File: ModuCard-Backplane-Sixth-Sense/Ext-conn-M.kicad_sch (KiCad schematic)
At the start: 1 part, among them J1 09031967921

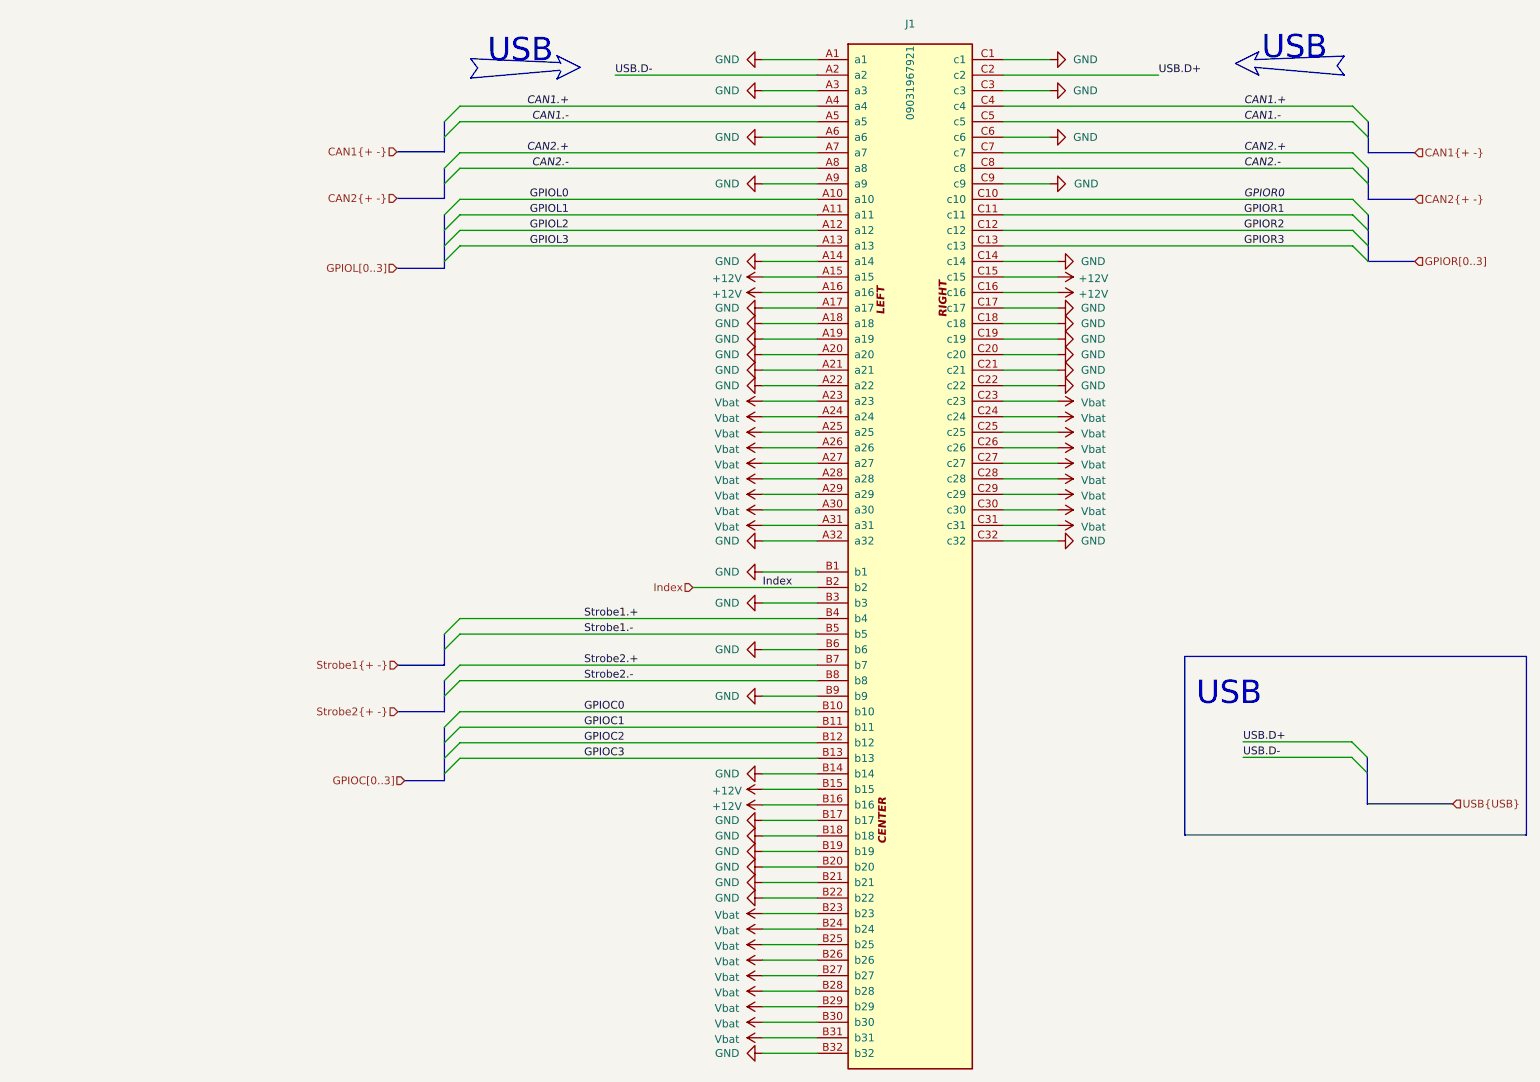
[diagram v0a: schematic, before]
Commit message: fix DRC errors, change pinout
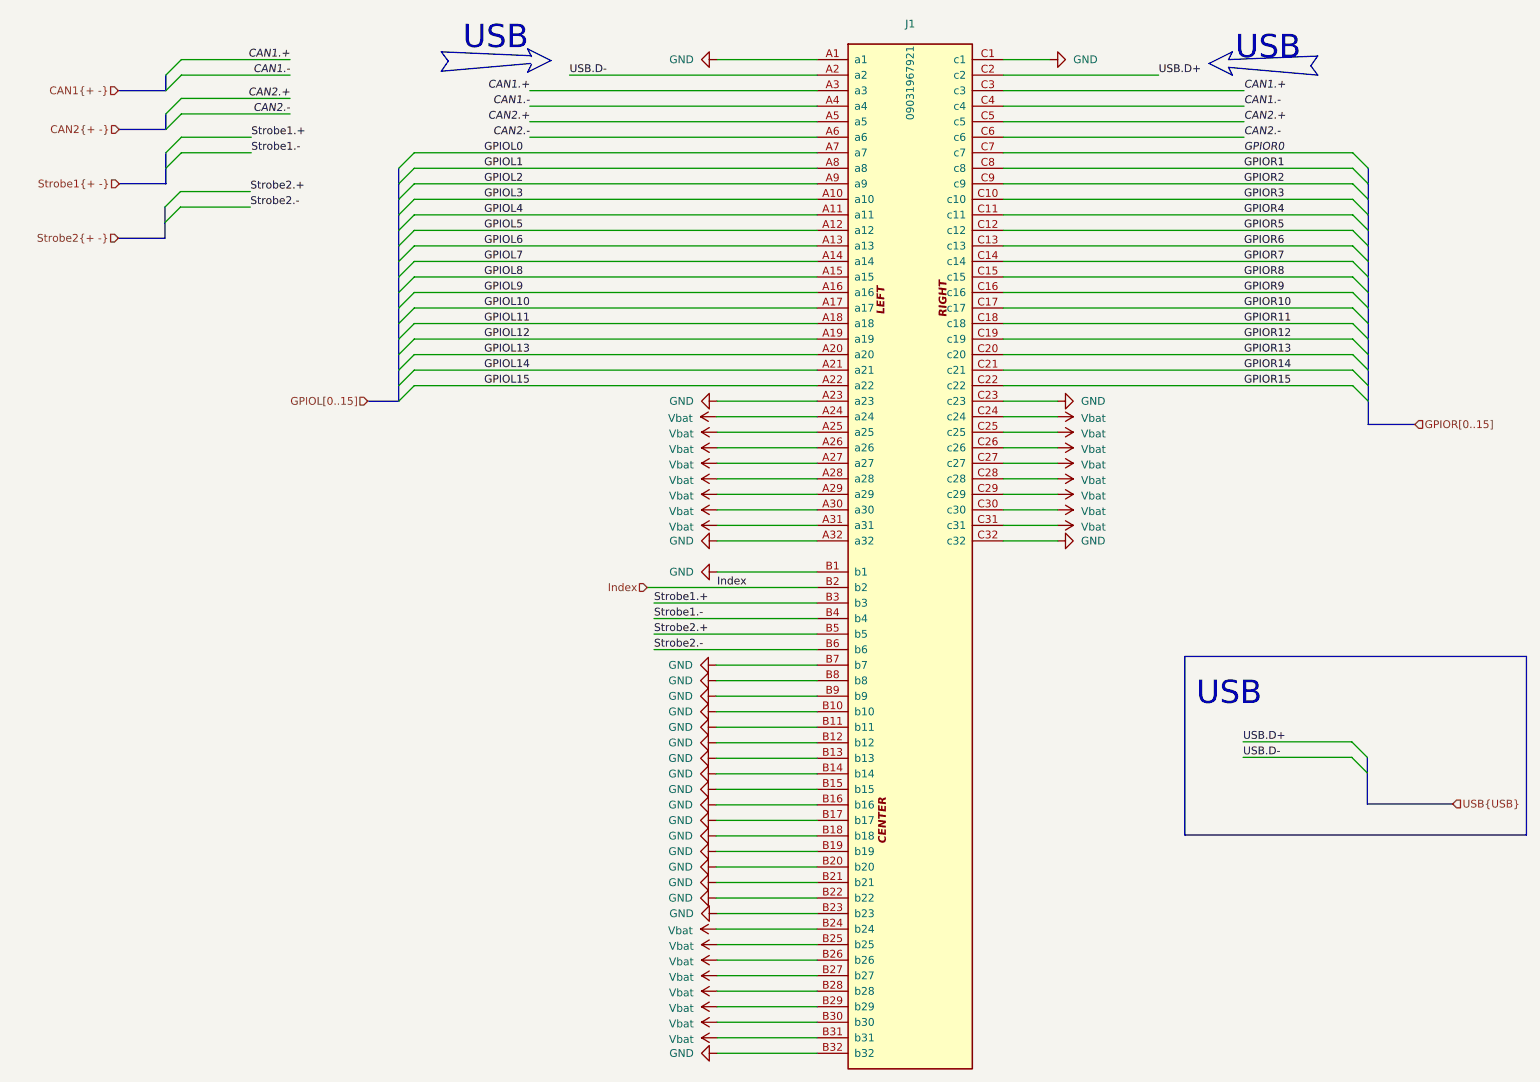
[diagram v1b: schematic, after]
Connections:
- net GPIOC0 is gone; now on net GND: J1.B10 (b10)
- net GPIOC1 is gone; now on net GND: J1.B11 (b11)
- net GPIOC2 is gone; now on net GND: J1.B12 (b12)
- net GPIOC3 is gone; now on net GND: J1.B13 (b13)
- net CAN1.+: now also J1.A3 (a3), J1.C3 (c3); no longer J1.A4 (a4), J1.C4 (c4)
- net CAN1.-: now also J1.A4 (a4), J1.C4 (c4); no longer J1.A5 (a5), J1.C5 (c5)
- net CAN2.+: now also J1.A5 (a5), J1.C5 (c5); no longer J1.A7 (a7), J1.C7 (c7)
- net CAN2.-: now also J1.A6 (a6), J1.C6 (c6); no longer J1.A8 (a8), J1.C8 (c8)
- net GND: now also J1.A23 (a23), J1.B15 (b15), J1.B16 (b16), J1.B23 (b23), J1.B7 (b7), J1.B8 (b8), J1.C23 (c23); no longer J1.A14 (a14), J1.A17 (a17), J1.A18 (a18), J1.A19 (a19), J1.A20 (a20), J1.A21 (a21), J1.A22 (a22), J1.A3 (a3), J1.A6 (a6), J1.A9 (a9), J1.B3 (b3), J1.B6 (b6), J1.C14 (c14), J1.C17 (c17), J1.C18 (c18), J1.C19 (c19), J1.C20 (c20), J1.C21 (c21), J1.C22 (c22), J1.C3 (c3), J1.C6 (c6), J1.C9 (c9)
- net GPIOL0: now also J1.A7 (a7); no longer J1.A10 (a10)
- net GPIOL1: now also J1.A8 (a8); no longer J1.A11 (a11)
- net GPIOL2: now also J1.A9 (a9); no longer J1.A12 (a12)
- net GPIOL3: now also J1.A10 (a10); no longer J1.A13 (a13)
- net GPIOR0: now also J1.C7 (c7); no longer J1.C10 (c10)
- net GPIOR1: now also J1.C8 (c8); no longer J1.C11 (c11)
- net GPIOR2: now also J1.C9 (c9); no longer J1.C12 (c12)
- net GPIOR3: now also J1.C10 (c10); no longer J1.C13 (c13)
- net Strobe1.+: now also J1.B3 (b3); no longer J1.B4 (b4)
- net Strobe1.-: now also J1.B4 (b4); no longer J1.B5 (b5)
- net Strobe2.+: now also J1.B5 (b5); no longer J1.B7 (b7)
- net Strobe2.-: now also J1.B6 (b6); no longer J1.B8 (b8)
- net Vbat: no longer J1.A23 (a23), J1.B23 (b23), J1.C23 (c23)
- removed net +12V: J1.A15 (a15), J1.A16 (a16), J1.B15 (b15), J1.B16 (b16), J1.C15 (c15), J1.C16 (c16)
- new net GPIOL10: J1.A17 (a17)
- new net GPIOL11: J1.A18 (a18)
- new net GPIOL12: J1.A19 (a19)
- new net GPIOL13: J1.A20 (a20)
- new net GPIOL14: J1.A21 (a21)
- new net GPIOL15: J1.A22 (a22)
- new net GPIOL4: J1.A11 (a11)
- new net GPIOL5: J1.A12 (a12)
- new net GPIOL6: J1.A13 (a13)
- new net GPIOL7: J1.A14 (a14)
- new net GPIOL8: J1.A15 (a15)
- new net GPIOL9: J1.A16 (a16)
- new net GPIOR10: J1.C17 (c17)
- new net GPIOR11: J1.C18 (c18)
- new net GPIOR12: J1.C19 (c19)
- new net GPIOR13: J1.C20 (c20)
- new net GPIOR14: J1.C21 (c21)
- new net GPIOR15: J1.C22 (c22)
- new net GPIOR4: J1.C11 (c11)
- new net GPIOR5: J1.C12 (c12)
- new net GPIOR6: J1.C13 (c13)
- new net GPIOR7: J1.C14 (c14)
- new net GPIOR8: J1.C15 (c15)
- new net GPIOR9: J1.C16 (c16)

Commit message: project overhaul
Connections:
- net GND: no longer J1.B1 (b1)
- net Index renamed Index2
- new net Index1: J1.B1 (b1)
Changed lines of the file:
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@@
 	)
 	(bus_entry
-		(at 23.0124 25.4)
+		(at 53.4924 137.16)
 		(size -2.54 2.54)
 		(stroke
@@
 	)
 	(bus_entry
-		(at 23.0124 22.86)
+		(at 53.4924 134.62)
 		(size -2.54 2.54)
 		(stroke
@@
 	)
 	(bus_entry
-		(at 20.4724 40.64)
+		(at 50.9524 152.4)
 		(size 2.54 -2.54)
 		(stroke
@@
 	)
 	(bus_entry
-		(at 20.32 49.53)
+		(at 50.8 161.29)
 		(size 2.54 -2.54)
 		(stroke
@@
 	)
 	(bus_entry
-		(at 20.32 46.99)
+		(at 50.8 158.75)
 		(size 2.54 -2.54)
 		(stroke
@@
 	)
 	(bus_entry
-		(at 23.0124 29.21)
+		(at 53.4924 140.97)
 		(size -2.54 2.54)
 		(stroke
@@
 	)
 	(bus_entry
-		(at 20.4724 38.1)
+		(at 50.9524 149.86)
 		(size 2.54 -2.54)
 		(stroke
@@
 	)
 	(bus_entry
-		(at 23.0124 31.75)
+		(at 53.4924 143.51)
 		(size -2.54 2.54)
 		(stroke
@@
 	(bus
 		(pts
-			(xy 12.8524 27.94) (xy 20.4724 27.94)
+			(xy 43.3324 139.7) (xy 50.9524 139.7)
 		)
 		(stroke
@@
 	(wire
 		(pts
+			(xy 99.2124 109.22) (xy 127 109.22)
+		)
+		(stroke
+			(width 0)
+			(type default)
+		)
+	)
+	(wire
+		(pts
 			(xy 166.37 99.06) (xy 157.48 99.06)
 		)
@@
 	(bus
 		(pts
-			(xy 20.4724 31.75) (xy 20.4724 34.29)
+			(xy 50.9524 143.51) (xy 50.9524 146.05)
 		)
 		(stroke
@@
 	(bus
 		(pts
-			(xy 20.32 46.99) (xy 20.32 49.53)
+			(xy 50.8 158.75) (xy 50.8 161.29)
 		)
 		(stroke
@@
 	(wire
 		(pts
-			(xy 23.0124 25.4) (xy 40.7924 25.4)
+			(xy 53.4924 137.16) (xy 71.2724 137.16)
 		)
 		(stroke
@@
 	(wire
 		(pts
-			(xy 23.0124 38.1) (xy 34.4424 38.1)
+			(xy 53.4924 149.86) (xy 64.9224 149.86)
 		)
 		(stroke
@@
 	(bus
 		(pts
-			(xy 20.32 49.53) (xy 20.32 52.07)
+			(xy 50.8 161.29) (xy 50.8 163.83)
 		)
 		(stroke
@@
 	(wire
 		(pts
-			(xy 22.86 44.45) (xy 34.29 44.45)
+			(xy 53.34 156.21) (xy 64.77 156.21)
 		)
 		(stroke
@@
 	(wire
 		(pts
-			(xy 196.85 35.56) (xy 157.48 35.56)
+			(xy 99.06 106.68) (xy 127 106.68)
 		)
 		(stroke
@@
 	(wire
 		(pts
-			(xy 110.49 81.28) (xy 127 81.28)
+			(xy 196.85 35.56) (xy 157.48 35.56)
 		)
 		(stroke
@@
 	(wire
 		(pts
-			(xy 166.37 96.52) (xy 157.48 96.52)
+			(xy 110.49 81.28) (xy 127 81.28)
 		)
 		(stroke
@@
 	(wire
 		(pts
-			(xy 166.37 93.98) (xy 157.48 93.98)
+			(xy 166.37 96.52) (xy 157.48 96.52)
 		)
 		(stroke
@@
 		)
 	)
-	(bus
+	(wire
 		(pts
-			(xy 58.5724 78.74) (xy 53.4924 78.74)
+			(xy 166.37 93.98) (xy 157.48 93.98)
 		)
 		(stroke
@@
 	(bus
 		(pts
-			(xy 12.8524 43.18) (xy 20.4724 43.18)
+			(xy 58.5724 78.74) (xy 53.4924 78.74)
 		)
 		(stroke
@@
 		)
 	)
-	(wire
+	(bus
 		(pts
-			(xy 80.01 27.94) (xy 127 27.94)
+			(xy 43.3324 154.94) (xy 50.9524 154.94)
 		)
 		(stroke
@@
 	(wire
 		(pts
-			(xy 99.2124 109.22) (xy 127 109.22)
+			(xy 80.01 27.94) (xy 127 27.94)
 		)
 		(stroke
@@
 	(wire
 		(pts
-			(xy 23.0124 35.56) (xy 34.4424 35.56)
+			(xy 53.4924 147.32) (xy 64.9224 147.32)
 		)
 		(stroke
@@
 	(bus
 		(pts
-			(xy 20.4724 40.64) (xy 20.4724 43.18)
+			(xy 50.9524 152.4) (xy 50.9524 154.94)
 		)
 		(stroke
@@
 	(wire
 		(pts
-			(xy 22.86 46.99) (xy 34.29 46.99)
+			(xy 53.34 158.75) (xy 64.77 158.75)
 		)
 		(stroke
@@
 	(bus
 		(pts
-			(xy 12.8524 34.29) (xy 20.4724 34.29)
+			(xy 43.3324 146.05) (xy 50.9524 146.05)
 		)
 		(stroke
@@
 	(bus
 		(pts
-			(xy 12.7 52.07) (xy 20.32 52.07)
+			(xy 43.18 163.83) (xy 50.8 163.83)
 		)
 		(stroke
@@
 	(wire
 		(pts
-			(xy 40.7924 29.21) (xy 23.0124 29.21)
+			(xy 71.2724 140.97) (xy 53.4924 140.97)
 		)
 		(stroke
@@
 	(wire
 		(pts
-			(xy 40.7924 31.75) (xy 23.0124 31.75)
-		)
-		(stroke
-			(width 0)
-			(type default)
-		)
-	)
-	(wire
-		(pts
-			(xy 110.6424 106.68) (xy 127 106.68)
+			(xy 71.2724 143.51) (xy 53.4924 143.51)
 		)
 		(stroke
@@
 	(bus
 		(pts
-			(xy 20.4724 38.1) (xy 20.4724 40.64)
+			(xy 50.9524 149.86) (xy 50.9524 152.4)
 		)
 		(stroke
@@
 	(wire
 		(pts
-			(xy 23.0124 22.86) (xy 40.7924 22.86)
+			(xy 53.4924 134.62) (xy 71.2724 134.62)
 		)
 		(stroke
@@
 	(bus
 		(pts
-			(xy 20.4724 25.4) (xy 20.4724 27.94)
+			(xy 50.9524 137.16) (xy 50.9524 139.7)
 		)
 		(stroke
@@
 	)
 	(label "CAN1.+"
-		(at 40.7924 22.86 180)
+		(at 71.2724 134.62 180)
 		(effects
 			(font
@@
 	)
 	(label "Strobe2.-"
-		(at 34.29 46.99 0)
+		(at 64.77 158.75 0)
 		(effects
 			(font
@@
 	)
 	(label "CAN2.-"
-		(at 40.7924 31.75 180)
+		(at 71.2724 143.51 180)
 		(effects
 			(font
@@
 	)
 	(label "CAN1.-"
-		(at 40.7924 25.4 180)
+		(at 71.2724 137.16 180)
 		(effects
 			(font
@@
 	)
 	(label "Strobe1.+"
-		(at 34.4424 35.56 0)
+		(at 64.9224 147.32 0)
 		(effects
 			(font
@@
 	)
 	(label "Strobe1.-"
-		(at 34.4424 38.1 0)
+		(at 64.9224 149.86 0)
 		(effects
 			(font
@@
 	)
 	(label "CAN2.+"
-		(at 40.7924 29.21 180)
+		(at 71.2724 140.97 180)
 		(effects
 			(font
@@
 		)
 	)
+	(label "Index1"
+		(at 100.1776 106.68 0)
+		(effects
+			(font
+				(size 1.27 1.27)
+			)
+			(justify left bottom)
+		)
+	)
 	(label "GPIOR14"
 		(at 196.85 73.66 0)
@@
 		)
 	)
-	(label "Index"
-		(at 110.6424 109.22 0)
+	(label "Index2"
+		(at 100.33 109.22 0)
 		(effects
 			(font
@@
 	)
 	(label "Strobe2.+"
-		(at 34.29 44.45 0)
+		(at 64.77 156.21 0)
 		(effects
 			(font
@@
 	(hierarchical_label "Strobe2{+ -}"
 		(shape input)
-		(at 12.7 52.07 180)
+		(at 43.18 163.83 180)
 		(effects
 			(font
@@
 		)
 	)
-	(hierarchical_label "Index"
-		(shape input)
-		(at 99.2124 109.22 180)
-		(effects
-			(font
-				(size 1.27 1.27)
-			)
-			(justify right)
-		)
-	)
 	(hierarchical_label "CAN2{+ -}"
 		(shape input)
-		(at 12.8524 34.29 180)
+		(at 43.3324 146.05 180)
 		(effects
 			(font
@@
 	(hierarchical_label "Strobe1{+ -}"
 		(shape input)
-		(at 12.8524 43.18 180)
+		(at 43.3324 154.94 180)
+		(effects
+			(font
+				(size 1.27 1.27)
+			)
+			(justify right)
+		)
+	)
+	(hierarchical_label "Index2"
+		(shape bidirectional)
+		(at 99.2124 109.22 180)
+		(effects
+			(font
+				(size 1.27 1.27)
+			)
+			(justify right)
+		)
+	)
+	(hierarchical_label "Index1"
+		(shape bidirectional)
+		(at 99.06 106.68 180)
 		(effects
 			(font
@@
 	(hierarchical_label "CAN1{+ -}"
 		(shape input)
-		(at 12.7 27.94 180)
+		(at 43.18 139.7 180)
 		(effects
 			(font
@@
 					(unit 1)
 				)
-			)
-		)
-	)
-	(symbol
-		(lib_id "power:GND")
-		(at 110.6424 106.68 270)
-		(unit 1)
-		(body_style 1)
-		(exclude_from_sim no)
-		(in_bom yes)
-		(on_board yes)
-		(in_pos_files yes)
-		(dnp no)
-		(fields_autoplaced yes)
-		(property "Reference" "#PWR0210"
-			(at 104.2924 106.68 0)
-			(hide yes)
-			(show_name no)
-			(do_not_autoplace no)
-			(effects
-				(font
-					(size 1.27 1.27)
-				)
-			)
-		)
-		(property "Value" "GND"
-			(at 106.8324 106.6799 90)
-			(show_name no)
-			(do_not_autoplace no)
-			(effects
-				(font
-					(size 1.27 1.27)
-				)
-				(justify right)
-			)
-		)
-		(property "Footprint" ""
-			(at 110.6424 106.68 0)
-			(hide yes)
-			(show_name no)
-			(do_not_autoplace no)
-			(effects
-				(font
-					(size 1.27 1.27)
-				)
-			)
-		)
-		(property "Datasheet" ""
-			(at 110.6424 106.68 0)
-			(hide yes)
-			(show_name no)
-			(do_not_autoplace no)
-			(effects
-				(font
-					(size 1.27 1.27)
-				)
-			)
-		)
-		(property "Description" "Power symbol creates a global label with name \"GND\" , ground"
-			(at 110.6424 106.68 0)
-			(hide yes)
-			(show_name no)
-			(do_not_autoplace no)
-			(effects
-				(font
-					(size 1.27 1.27)
-				)
-			)
-		)
-		(pin "1"
-		)
-		(instances
-			(project "ModuCard-Backplane-Sixth-Sense"
-				(path "/b8e6d233-63ab-459d-a617-f62d9ba23c71/1b39a8b3-369e-487c-a41c-a98469e8eb80"
-					(reference "#PWR0210")
-					(unit 1)
-				)
